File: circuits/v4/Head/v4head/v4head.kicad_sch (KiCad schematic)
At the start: 20 parts, among them J1 Raspberry_Pi_2_3

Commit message: Updates to circuit
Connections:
- net +5V: now also J1.4 (5V)
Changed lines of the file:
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@@
   (junction (at 242.57 93.98) (diameter 0) (color 0 0 0 0)
   )
+  (junction (at 96.52 77.47) (diameter 0) (color 0 0 0 0)
+  )
   (junction (at 187.96 109.22) (diameter 0) (color 0 0 0 0)
   )
@@
     (stroke (width 0) (type default))
   )
+  (wire (pts (xy 96.52 77.47) (xy 99.06 77.47))
+    (stroke (width 0) (type default))
+  )

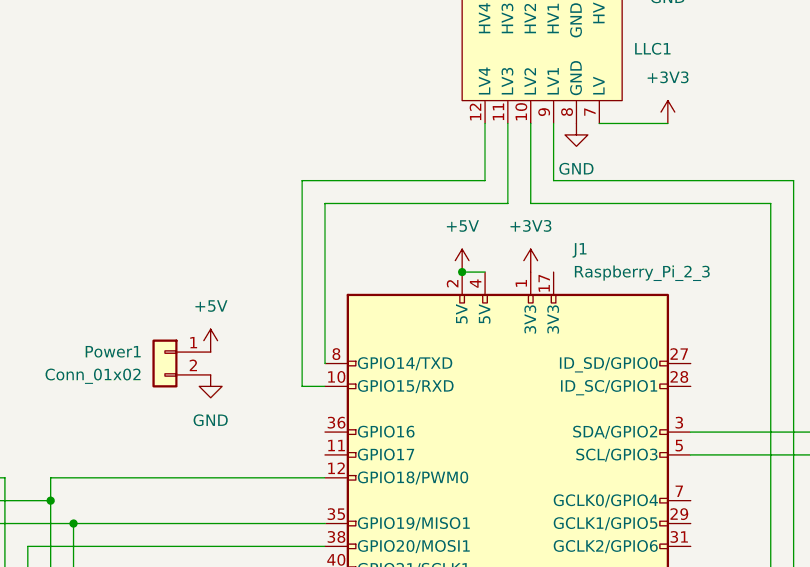
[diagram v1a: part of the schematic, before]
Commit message: Swap TX & RX to align with LLC
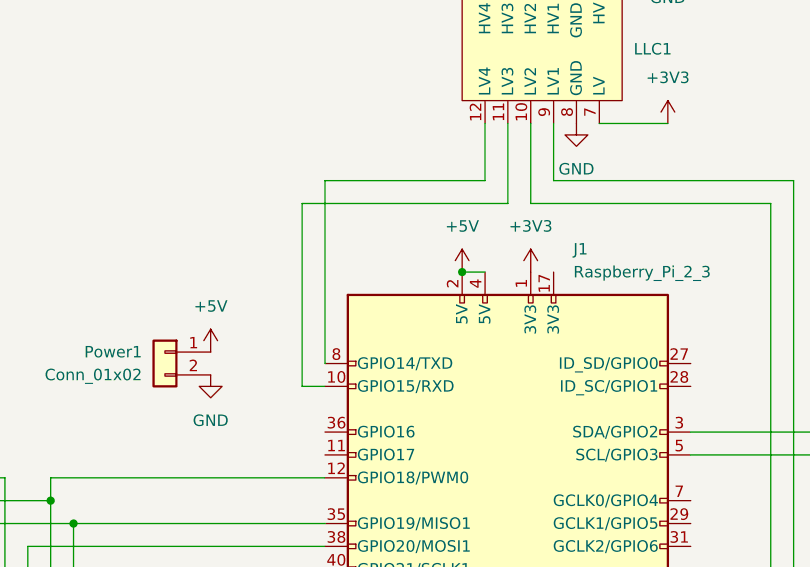
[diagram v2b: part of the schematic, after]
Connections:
- net at J1.10 (GPIO15/RXD): now also LLC1.11 (LV3); no longer LLC1.12 (LV4)
- net at J1.8 (GPIO14/TXD): now also LLC1.12 (LV4); no longer LLC1.11 (LV3)

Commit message: Update annotations
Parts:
- renumbered 3VMODULE1 to 3V_EXT1, 5VMODULE1 to 5V_EXT1, I2CMODULE1 to I2C_EXT1, NEO1 to I2C_NEO1, NEO2 to NEO1, J1 to PI1, Power1 to PWR1, RCWL-1 to RCWL-516, Serial2 to SERIAL1
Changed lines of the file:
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@@
   (symbol (lib_id "ComponentLibrary:RCWL-0516") (at 64.77 146.05 0) (mirror y) (unit 1)
     (in_bom yes) (on_board yes) (dnp no)
-    (property "Reference" "RCWL-1" (at 60.96 151.13 0)
+    (property "Reference" "RCWL-516" (at 60.96 151.13 0)
       (effects (font (size 1.27 1.27)) (justify left))
     )
@@
       (project "v4head"
         (path "/6f9ecdea-83ce-4770-aa87-96e479963d0e"
-          (reference "RCWL-1") (unit 1)
+          (reference "RCWL-516") (unit 1)
         )
       )
@@
   (symbol (lib_id "Connector_Generic:Conn_01x03") (at 119.38 33.02 0) (unit 1)
     (in_bom yes) (on_board yes) (dnp no)
-    (property "Reference" "5VMODULE1" (at 121.92 31.75 0)
+    (property "Reference" "5V_EXT1" (at 121.92 31.75 0)
       (effects (font (size 1.27 1.27)) (justify left))
     )
@@
       (project "v4head"
         (path "/6f9ecdea-83ce-4770-aa87-96e479963d0e"
-          (reference "5VMODULE1") (unit 1)
+          (reference "5V_EXT1") (unit 1)
         )
       )
@@
   (symbol (lib_id "Connector_Generic:Conn_01x02") (at 63.5 86.36 0) (mirror y) (unit 1)
     (in_bom yes) (on_board yes) (dnp no)
-    (property "Reference" "Power1" (at 60.96 86.36 0)
+    (property "Reference" "PWR1" (at 60.96 86.36 0)
       (effects (font (size 1.27 1.27)) (justify left))
     )
@@
       (project "v4head"
         (path "/6f9ecdea-83ce-4770-aa87-96e479963d0e"
-          (reference "Power1") (unit 1)
+          (reference "PWR1") (unit 1)
         )
       )
@@
   (symbol (lib_id "Connector_Generic:Conn_01x03") (at 275.59 101.6 0) (unit 1)
     (in_bom yes) (on_board yes) (dnp no)
-    (property "Reference" "NEO2" (at 271.78 106.68 0)
+    (property "Reference" "NEO1" (at 271.78 106.68 0)
       (effects (font (size 1.27 1.27)) (justify left))
     )
@@
       (project "v4head"
         (path "/6f9ecdea-83ce-4770-aa87-96e479963d0e"
-          (reference "NEO2") (unit 1)
+          (reference "NEO1") (unit 1)
         )
       )
@@
   (symbol (lib_id "Connector_Generic:Conn_01x03") (at 57.15 125.73 0) (mirror y) (unit 1)
     (in_bom yes) (on_board yes) (dnp no)
-    (property "Reference" "3VMODULE1" (at 66.04 116.84 0)
+    (property "Reference" "3V_EXT1" (at 66.04 116.84 0)
       (effects (font (size 1.27 1.27)) (justify left))
     )
@@
       (project "v4head"
         (path "/6f9ecdea-83ce-4770-aa87-96e479963d0e"
-          (reference "3VMODULE1") (unit 1)
+          (reference "3V_EXT1") (unit 1)
         )
       )
@@
   (symbol (lib_id "Connector:Raspberry_Pi_2_3") (at 101.6 110.49 0) (unit 1)
     (in_bom yes) (on_board yes) (dnp no) (fields_autoplaced)
-    (property "Reference" "J1" (at 108.8741 74.93 0)
+    (property "Reference" "PI1" (at 108.8741 74.93 0)
       (effects (font (size 1.27 1.27)) (justify left))
     )
@@
       (project "v4head"
         (path "/6f9ecdea-83ce-4770-aa87-96e479963d0e"
-          (reference "J1") (unit 1)
+          (reference "PI1") (unit 1)
         )
       )
@@
   (symbol (lib_id "Connector_Generic:Conn_01x02") (at 93.98 41.91 0) (mirror y) (unit 1)
     (in_bom yes) (on_board yes) (dnp no)
-    (property "Reference" "Serial2" (at 91.44 41.91 0)
+    (property "Reference" "SERIAL1" (at 91.44 41.91 0)
       (effects (font (size 1.27 1.27)) (justify left))
     )
@@
       (project "v4head"
         (path "/6f9ecdea-83ce-4770-aa87-96e479963d0e"
-          (reference "Serial2") (unit 1)
+          (reference "SERIAL1") (unit 1)
         )
       )
@@
   (symbol (lib_id "Connector_Generic:Conn_01x04") (at 158.75 130.81 0) (unit 1)
     (in_bom yes) (on_board yes) (dnp no) (fields_autoplaced)
-    (property "Reference" "I2CMODULE1" (at 161.29 130.81 0)
+    (property "Reference" "I2C_EXT1" (at 161.29 130.81 0)
       (effects (font (size 1.27 1.27)) (justify left))
     )
@@
       (project "v4head"
         (path "/6f9ecdea-83ce-4770-aa87-96e479963d0e"
-          (reference "I2CMODULE1") (unit 1)
+          (reference "I2C_EXT1") (unit 1)
         )
       )
@@
   (symbol (lib_id "ComponentLibrary:I2C_NEOPIXEL") (at 160.02 93.98 0) (unit 1)
     (in_bom yes) (on_board yes) (dnp no)
-    (property "Reference" "NEO1" (at 170.18 91.44 90)
+    (property "Reference" "I2C_NEO1" (at 170.18 96.52 90)
       (effects (font (size 1.27 1.27)) (justify left))
     )
@@
       (project "v4head"
         (path "/6f9ecdea-83ce-4770-aa87-96e479963d0e"
-          (reference "NEO1") (unit 1)
-        )
-      )
+          (reference "I2C_NEO1") (unit 1)
+        )
+      )

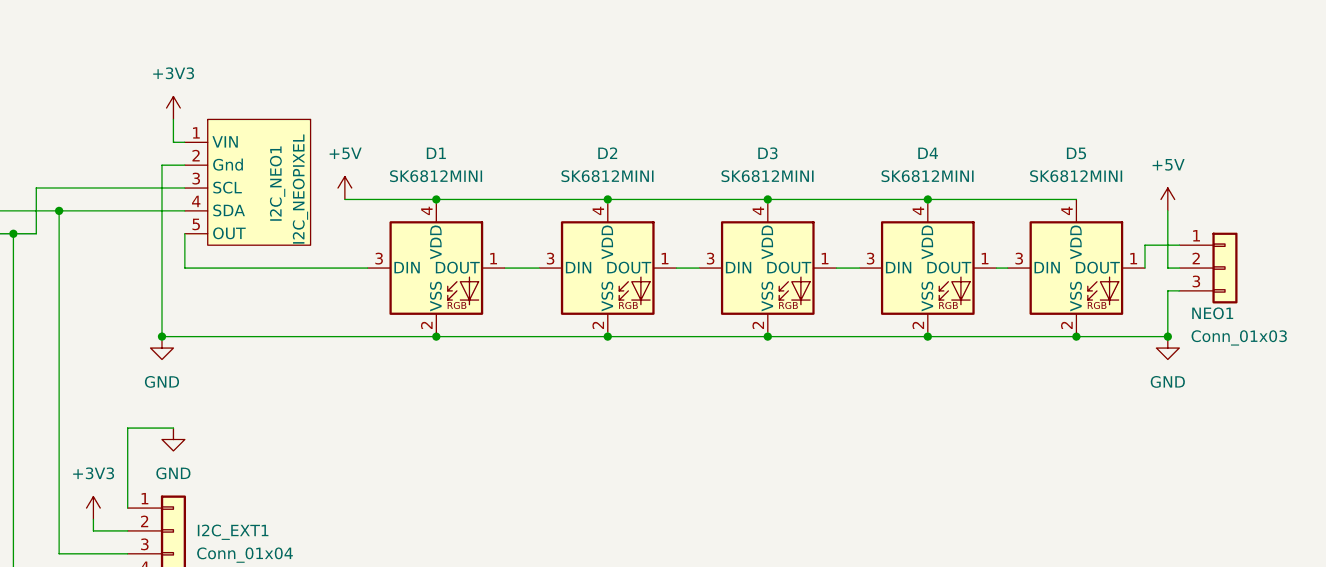
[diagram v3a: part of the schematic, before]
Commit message: Final version 1.0. Added decoupling caps to neopixels.
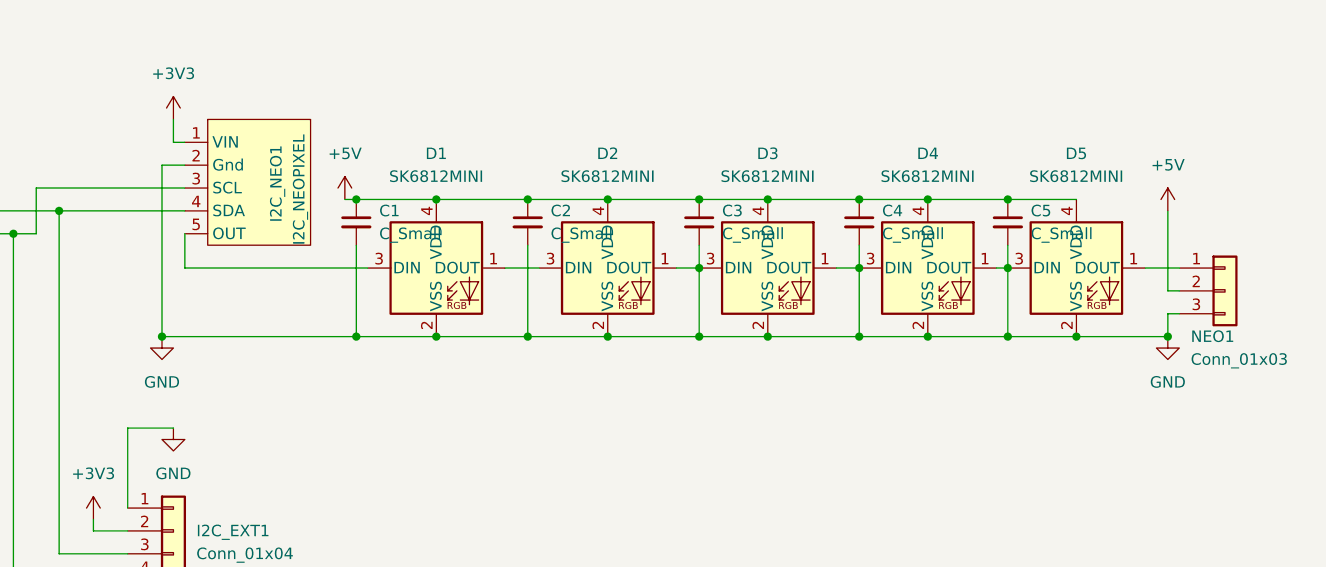
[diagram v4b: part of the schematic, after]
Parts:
- added C1, C2, C3, C4, C5: C_Small, Capacitor_SMD:C_0201_0603Metric, symbol Device:C_Small
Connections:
- net +5V: now also C1.1, C2.1, C3.1, C4.1, C5.1
- net GND: now also D2.1 (DOUT), D3.1 (DOUT), D3.3 (DIN), D4.1 (DOUT), D4.3 (DIN), D5.3 (DIN), C1.2, C2.2, C3.2, C4.2, C5.2
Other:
- moved on the sheet: NEO1
